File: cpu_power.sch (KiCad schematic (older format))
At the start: 81 parts

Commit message: annotation, wip erc
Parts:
- removed C? (x4): 100nF/6.3V, symbol C
- added C70, C72, C74, C75: 100nF/6.3V, symbol C
- gave numbers to parts that had none: 77

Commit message: erc passed, sch first version
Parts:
- W1: value VDD_MPUON -> VDD_MPU_MON
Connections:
- wire segments 234 -> 238
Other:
- note added: "VDD_MPU_MON connected to VDD_MPU \naccording to Fig 6-7 of AM335x datasheet."
- moved on the sheet: W1

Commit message: wip sys and power
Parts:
- removed C100, C101, C102, C103, C104, C105, C106, C107, C108, C109, C110, C43, C45, C46, C48, C50, C51, C52, C53, C54, C55, C56, C57, C58, C59, C60, C61, C62, C63, C64, C65, C66, C67, C68, C69, C70, C71, C72, C73, C74, C75, C77, C78, C79, C80, C81, C82, C83, C84, C86, C87, C88, C89, C90, C91, C92, C94, C96, C97, C98, C99: 100nF/6.3V, symbol C
- removed C111, C112, C113, C114, C115: 1uF/10V, symbol C
- removed C44, C47, C76, C85, C93, C95: 10uF/10V, symbol C
- removed C49: 1nF/50V, symbol C
- removed IC2: AM335X_ZCZ, symbol AM335X_ZCZ
- removed L5, L6, L7: 150OHM800mA, symbol L
- removed R29, R30, R31: 0R, symbol R
- removed W1: VDD_MPU_MON, symbol TEST_1P
- added IC? (x2): OSD335x, GHI-SoMs-Processors_OSD3358, symbol OSD335x
- added R?: 10k 1%, symbol R
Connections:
- net labels removed: GND_OSC, VDDS, VSS_RTC
- wire segments 238 -> 104
- no-connect marks 1 -> 65
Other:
- note removed: "VDD_MPU_MON connected to VDD_MPU \naccording to Fig 6-7 of AM335x datasheet."

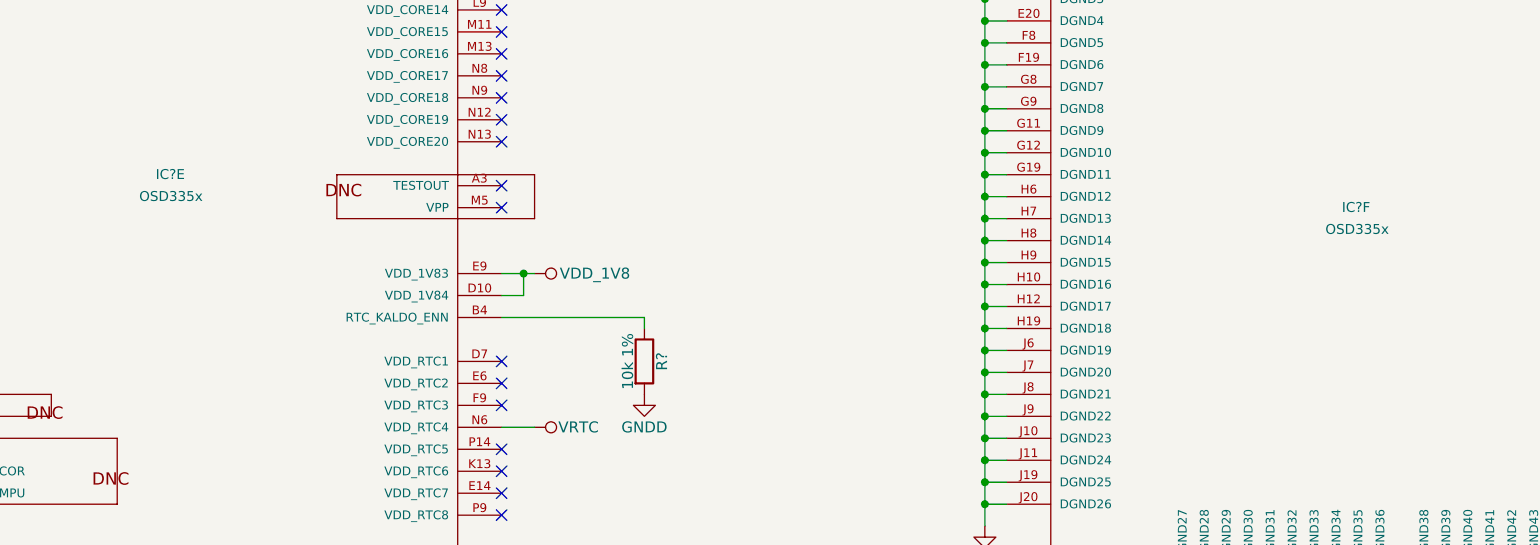
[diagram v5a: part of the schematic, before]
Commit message: only io connectors remaining
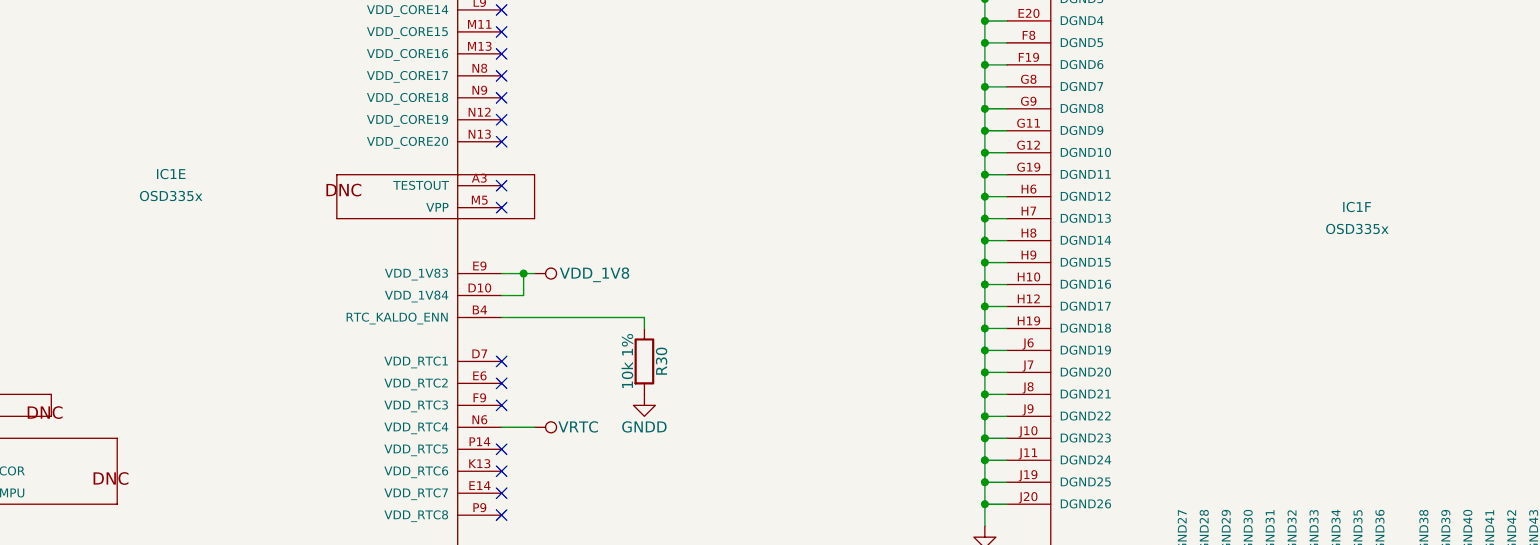
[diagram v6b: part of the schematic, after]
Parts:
- gave numbers to parts that had none: 2
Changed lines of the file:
@@
 $Descr A4 11693 8268
 encoding utf-8
-Sheet 5 6
+Sheet 4 6
 Title ""
 Date ""
@@
 $EndDescr
 $Comp
-L OSD335x IC?
+L OSD335x IC1
 U 5 1 58DDF956
 P 3200 3550
-F 0 "IC?" H 3125 3575 45  0000 L BNN
+F 0 "IC1" H 3125 3575 45  0000 L BNN
 F 1 "OSD335x" H 3050 3475 45  0000 L BNN
 F 2 "GHI-SoMs-Processors_OSD3358" H 3230 3700 20  0001 C CNN
@@
 $EndComp
 $Comp
-L OSD335x IC?
+L OSD335x IC1
 U 6 1 58DDF9B7
 P 8600 3700
-F 0 "IC?" H 8525 3725 45  0000 L BNN
+F 0 "IC1" H 8525 3725 45  0000 L BNN
 F 1 "OSD335x" H 8450 3625 45  0000 L BNN
 F 2 "GHI-SoMs-Processors_OSD3358" H 8630 3850 20  0001 C CNN
@@
 	6900 5000 7000 5000
 $Comp
-L GNDD #PWR?
+L GNDD #PWR66
 U 1 1 58E11DA7
 P 6900 5100
-F 0 "#PWR?" H 6900 4850 50  0001 C CNN
+F 0 "#PWR66" H 6900 4850 50  0001 C CNN
 F 1 "GNDD" H 6900 4950 50  0000 C CNN
 F 2 "" H 6900 5100 50  0001 C CNN
@@
 	10300 5000 10200 5000
 $Comp
-L GNDD #PWR?
+L GNDD #PWR69
 U 1 1 58E11EBE
 P 10300 5100
-F 0 "#PWR?" H 10300 4850 50  0001 C CNN
+F 0 "#PWR69" H 10300 4850 50  0001 C CNN
 F 1 "GNDD" H 10300 4950 50  0000 C CNN
 F 2 "" H 10300 5100 50  0001 C CNN
@@
 	7800 5500 7800 5650
 $Comp
-L GNDD #PWR?
+L GNDD #PWR67
 U 1 1 58E12353
 P 7800 5650
-F 0 "#PWR?" H 7800 5400 50  0001 C CNN
+F 0 "#PWR67" H 7800 5400 50  0001 C CNN
 F 1 "GNDD" H 7800 5500 50  0000 C CNN
 F 2 "" H 7800 5650 50  0001 C CNN
@@
 Connection ~ 7800 5600
 $Comp
-L GNDA #PWR?
+L GNDA #PWR68
 U 1 1 58E12456
 P 9700 5600
-F 0 "#PWR?" H 9700 5350 50  0001 C CNN
+F 0 "#PWR68" H 9700 5350 50  0001 C CNN
 F 1 "GNDA" H 9700 5450 50  0000 C CNN
 F 2 "" H 9700 5600 50  0001 C CNN
@@
 Connection ~ 1600 2950
 $Comp
-L VDD_3V3A #PWR?
+L VDD_3V3A #PWR57
 U 1 1 58E148B3
 P 1400 2850
-F 0 "#PWR?" H 1400 2700 50  0001 C CNN
+F 0 "#PWR57" H 1400 2700 50  0001 C CNN
 F 1 "VDD_3V3A" V 1400 3150 50  0000 C CNN
 F 2 "" H 1400 2850 50  0000 C CNN
@@
 Connection ~ 1600 2850
 $Comp
-L VDD_MPU #PWR?
+L VDD_MPU #PWR60
 U 1 1 58E14A82
 P 1600 3750
-F 0 "#PWR?" H 1600 3600 50  0001 C CNN
+F 0 "#PWR60" H 1600 3600 50  0001 C CNN
 F 1 "VDD_MPU" V 1600 4025 50  0000 C CNN
 F 2 "" H 1600 3750 50  0000 C CNN
@@
 	1600 3750 1700 3750
 $Comp
-L VDD_ADC #PWR?
+L VDD_ADC #PWR58
 U 1 1 58E14B9C
 P 1400 5050
-F 0 "#PWR?" H 1400 4900 50  0001 C CNN
+F 0 "#PWR58" H 1400 4900 50  0001 C CNN
 F 1 "VDD_ADC" V 1400 5325 50  0000 C CNN
 F 2 "" H 1400 5050 50  0000 C CNN
@@
 	1700 5050 1400 5050
 $Comp
-L VDD_PLL #PWR?
+L VDD_PLL #PWR59
 U 1 1 58E14C7B
 P 1400 5250
-F 0 "#PWR?" H 1400 5100 50  0001 C CNN
+F 0 "#PWR59" H 1400 5100 50  0001 C CNN
 F 1 "VDD_PLL" V 1400 5525 50  0000 C CNN
 F 2 "" H 1400 5250 50  0000 C CNN
@@
 NoConn ~ 1700 4950
 $Comp
-L VDD_CORE #PWR?
+L VDD_CORE #PWR64
 U 1 1 58E150D4
 P 4900 1450
-F 0 "#PWR?" H 4900 1300 50  0001 C CNN
+F 0 "#PWR64" H 4900 1300 50  0001 C CNN
 F 1 "VDD_CORE" V 4900 1750 50  0000 C CNN
 F 2 "" H 4900 1450 50  0000 C CNN
@@
 NoConn ~ 4700 3650
 $Comp
-L VRTC #PWR?
+L VRTC #PWR62
 U 1 1 58E1525D
 P 4850 4650
-F 0 "#PWR?" H 4850 4500 50  0001 C CNN
+F 0 "#PWR62" H 4850 4500 50  0001 C CNN
 F 1 "VRTC" V 4850 4850 50  0000 C CNN
 F 2 "" H 4850 4650 50  0000 C CNN
@@
 	4850 4650 4700 4650
 $Comp
-L R R?
+L R R30
 U 1 1 58E1536B
 P 5350 4350
-F 0 "R?" V 5430 4350 50  0000 C CNN
+F 0 "R30" V 5430 4350 50  0000 C CNN
 F 1 "10k 1%" V 5275 4350 50  0000 C CNN
 F 2 "" V 5280 4350 50  0001 C CNN
@@
 $EndComp
 $Comp
-L GNDD #PWR?
+L GNDD #PWR65
 U 1 1 58E153CC
 P 5350 4500
-F 0 "#PWR?" H 5350 4250 50  0001 C CNN
+F 0 "#PWR65" H 5350 4250 50  0001 C CNN
 F 1 "GNDD" H 5350 4350 50  0000 C CNN
 F 2 "" H 5350 4500 50  0001 C CNN
@@
 NoConn ~ 4700 5050
 $Comp
-L VDDS_DDR #PWR?
+L VDDS_DDR #PWR63
 U 1 1 58E1559B
 P 4850 5550
-F 0 "#PWR?" H 4850 5400 50  0001 C CNN
+F 0 "#PWR63" H 4850 5400 50  0001 C CNN
 F 1 "VDDS_DDR" V 4850 5850 50  0000 C CNN
 F 2 "" H 4850 5550 50  0000 C CNN
@@
 NoConn ~ 4700 5850
 $Comp
-L VDD_1V8 #PWR?
+L VDD_1V8 #PWR61
 U 1 1 58E16271
 P 4850 3950
-F 0 "#PWR?" H 4850 3800 50  0001 C CNN
+F 0 "#PWR61" H 4850 3800 50  0001 C CNN
 F 1 "VDD_1V8" V 4850 4225 50  0000 C CNN
 F 2 "" H 4850 3950 50  0000 C CNN

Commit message: erc passed
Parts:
- added J15: VDDS_PLL, symbol TEST_1P
- added J16: VDDS_DDR, symbol TEST_1P
- added J17: VDD_MPU, symbol TEST_1P
- added J18: VDD_CORE, symbol TEST_1P
- IC1: symbol OSD335x -> OSD335x-RESCUE-mateboard
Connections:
- net VDDS_DDR: no longer names the net of IC1.H5 (VDDS_DDR4)
- net VDDS_DDR: now also J16.1
- net VDD_CORE: no longer names the net of IC1.F6 (VDD_CORE1)
- net VDD_CORE: now also J18.1
- net VDD_MPU: no longer names the net of IC1.F10 (VDD_MPU0)
- net VDD_MPU: now also J17.1
- net VDD_PLL: no longer names the net of IC1.E7 (VDD_PLL1)
- net VDD_PLL: now also J15.1
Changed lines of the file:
@@
 $EndDescr
 $Comp
-L OSD335x IC1
+L OSD335x-RESCUE-mateboard IC1
 U 5 1 58DDF956
 P 3200 3550
+AR Path="/58DDF956" Ref="IC1"  Part="5"
+AR Path="/589E2993/58DDF956" Ref="IC1"  Part="5"
 F 0 "IC1" H 3125 3575 45  0000 L BNN
 F 1 "OSD335x" H 3050 3475 45  0000 L BNN
@@
 $EndComp
 $Comp
-L OSD335x IC1
+L OSD335x-RESCUE-mateboard IC1
 U 6 1 58DDF9B7
 P 8600 3700
+AR Path="/58DDF9B7" Ref="IC1"  Part="6"
+AR Path="/589E2993/58DDF9B7" Ref="IC1"  Part="6"
 F 0 "IC1" H 8525 3725 45  0000 L BNN
 F 1 "OSD335x" H 8450 3625 45  0000 L BNN
@@
 	6900 5000 7000 5000
 $Comp
-L GNDD #PWR66
+L GNDD #PWR094
 U 1 1 58E11DA7
 P 6900 5100
-F 0 "#PWR66" H 6900 4850 50  0001 C CNN
+F 0 "#PWR094" H 6900 4850 50  0001 C CNN
 F 1 "GNDD" H 6900 4950 50  0000 C CNN
 F 2 "" H 6900 5100 50  0001 C CNN
@@
 	10300 5000 10200 5000
 $Comp
-L GNDD #PWR69
+L GNDD #PWR095
 U 1 1 58E11EBE
 P 10300 5100
-F 0 "#PWR69" H 10300 4850 50  0001 C CNN
+F 0 "#PWR095" H 10300 4850 50  0001 C CNN
 F 1 "GNDD" H 10300 4950 50  0000 C CNN
 F 2 "" H 10300 5100 50  0001 C CNN
@@
 Connection ~ 9400 5600
 Wire Wire Line
-	9500 5500 9500 5600
-Wire Wire Line
-	9500 5600 7800 5600
+	9500 5600 9500 5500
+Wire Wire Line
+	7800 5600 9500 5600
 Wire Wire Line
 	7800 5500 7800 5650
 $Comp
-L GNDD #PWR67
+L GNDD #PWR096
 U 1 1 58E12353
 P 7800 5650
-F 0 "#PWR67" H 7800 5400 50  0001 C CNN
+F 0 "#PWR096" H 7800 5400 50  0001 C CNN
 F 1 "GNDD" H 7800 5500 50  0000 C CNN
 F 2 "" H 7800 5650 50  0001 C CNN
@@
 Connection ~ 7800 5600
 $Comp
-L GNDA #PWR68
+L GNDA #PWR097
 U 1 1 58E12456
 P 9700 5600
-F 0 "#PWR68" H 9700 5350 50  0001 C CNN
+F 0 "#PWR097" H 9700 5350 50  0001 C CNN
 F 1 "GNDA" H 9700 5450 50  0000 C CNN
 F 2 "" H 9700 5600 50  0001 C CNN
@@
 $EndComp
 Wire Wire Line
-	9700 5600 9700 5500
+	9700 5500 9700 5600
 Wire Wire Line
 	1600 3050 1700 3050
@@
 Connection ~ 1600 2950
 $Comp
-L VDD_3V3A #PWR57
+L VDD_3V3A #PWR098
 U 1 1 58E148B3
 P 1400 2850
-F 0 "#PWR57" H 1400 2700 50  0001 C CNN
+F 0 "#PWR098" H 1400 2700 50  0001 C CNN
 F 1 "VDD_3V3A" V 1400 3150 50  0000 C CNN
 F 2 "" H 1400 2850 50  0000 C CNN
@@
 $EndComp
 Connection ~ 1600 2850
-$Comp
-L VDD_MPU #PWR60
-U 1 1 58E14A82
-P 1600 3750
-F 0 "#PWR60" H 1600 3600 50  0001 C CNN
-F 1 "VDD_MPU" V 1600 4025 50  0000 C CNN
-F 2 "" H 1600 3750 50  0000 C CNN
-F 3 "" H 1600 3750 50  0000 C CNN
-	1    1600 3750
-	0    -1   -1   0
-$EndComp
-Wire Wire Line
-	1600 3750 1700 3750
-$Comp
-L VDD_ADC #PWR58
+Wire Wire Line
+	1550 3750 1700 3750
+$Comp
+L VDD_ADC #PWR099
 U 1 1 58E14B9C
 P 1400 5050
-F 0 "#PWR58" H 1400 4900 50  0001 C CNN
+F 0 "#PWR099" H 1400 4900 50  0001 C CNN
 F 1 "VDD_ADC" V 1400 5325 50  0000 C CNN
 F 2 "" H 1400 5050 50  0000 C CNN
@@
 Wire Wire Line
 	1700 5050 1400 5050
-$Comp
-L VDD_PLL #PWR59
-U 1 1 58E14C7B
-P 1400 5250
-F 0 "#PWR59" H 1400 5100 50  0001 C CNN
-F 1 "VDD_PLL" V 1400 5525 50  0000 C CNN
-F 2 "" H 1400 5250 50  0000 C CNN
-F 3 "" H 1400 5250 50  0000 C CNN
-	1    1400 5250
-	0    -1   -1   0
-$EndComp
 Wire Wire Line
 	1400 5250 1700 5250
@@
 NoConn ~ 1700 4850
 NoConn ~ 1700 4950
-$Comp
-L VDD_CORE #PWR64
-U 1 1 58E150D4
-P 4900 1450
-F 0 "#PWR64" H 4900 1300 50  0001 C CNN
-F 1 "VDD_CORE" V 4900 1750 50  0000 C CNN
-F 2 "" H 4900 1450 50  0000 C CNN
-F 3 "" H 4900 1450 50  0000 C CNN
-	1    4900 1450
-	0    1    1    0
-$EndComp
 Wire Wire Line
 	4900 1450 4700 1450
@@
 NoConn ~ 4700 3550
 NoConn ~ 4700 3650
-$Comp
-L VRTC #PWR62
-U 1 1 58E1525D
-P 4850 4650
-F 0 "#PWR62" H 4850 4500 50  0001 C CNN
-F 1 "VRTC" V 4850 4850 50  0000 C CNN
-F 2 "" H 4850 4650 50  0000 C CNN
-F 3 "" H 4850 4650 50  0000 C CNN
-	1    4850 4650
-	0    1    1    0
-$EndComp
 Wire Wire Line
 	4850 4650 4700 4650
@@
 $EndComp
 $Comp
-L GNDD #PWR65
+L GNDD #PWR0100
 U 1 1 58E153CC
 P 5350 4500
-F 0 "#PWR65" H 5350 4250 50  0001 C CNN
+F 0 "#PWR0100" H 5350 4250 50  0001 C CNN
 F 1 "GNDD" H 5350 4350 50  0000 C CNN
 F 2 "" H 5350 4500 50  0001 C CNN
@@
 NoConn ~ 4700 4950
 NoConn ~ 4700 5050
-$Comp
-L VDDS_DDR #PWR63
-U 1 1 58E1559B
-P 4850 5550
-F 0 "#PWR63" H 4850 5400 50  0001 C CNN
-F 1 "VDDS_DDR" V 4850 5850 50  0000 C CNN
-F 2 "" H 4850 5550 50  0000 C CNN
-F 3 "" H 4850 5550 50  0000 C CNN
-	1    4850 5550
-	0    1    1    0
-$EndComp
 Wire Wire Line
 	4850 5550 4700 5550
@@
 NoConn ~ 4700 5850
 $Comp
-L VDD_1V8 #PWR61
+L VDD_1V8 #PWR0101
 U 1 1 58E16271
 P 4850 3950
-F 0 "#PWR61" H 4850 3800 50  0001 C CNN
+F 0 "#PWR0101" H 4850 3800 50  0001 C CNN
 F 1 "VDD_1V8" V 4850 4225 50  0000 C CNN
 F 2 "" H 4850 3950 50  0000 C CNN
@@
 $EndComp
 Wire Wire Line
-	4850 3950 4700 3950
+	4700 3950 4850 3950
 Wire Wire Line
 	4800 3950 4800 4050
@@
 	4800 4050 4700 4050
 Connection ~ 4800 3950
+$Comp
+L PWR_FLAG #FLG0102
+U 1 1 58DCC8EE
+P 9700 5550
+F 0 "#FLG0102" H 9700 5625 50  0001 C CNN
+F 1 "PWR_FLAG" H 9700 5700 50  0001 C CNN
+F 2 "" H 9700 5550 50  0001 C CNN
+F 3 "" H 9700 5550 50  0001 C CNN
+	1    9700 5550
+	0    1    1    0
+$EndComp
+Connection ~ 9700 5550
+$Comp
+L TEST_1P J15
+U 1 1 58DD0E89
+P 1400 5250
+F 0 "J15" V 1425 5300 50  0000 C CNN
+F 1 "VDDS_PLL" V 1400 5600 50  0000 C CNN
+F 2 "" H 1600 5250 50  0001 C CNN
+F 3 "" H 1600 5250 50  0001 C CNN
+	1    1400 5250
+	0    -1   -1   0
+$EndComp
+$Comp
+L TEST_1P J16
+U 1 1 58DD1032
+P 4850 5550
+F 0 "J16" V 4800 5600 50  0000 C CNN
+F 1 "VDDS_DDR" V 4850 5925 50  0000 C CNN
+F 2 "" H 5050 5550 50  0001 C CNN
+F 3 "" H 5050 5550 50  0001 C CNN
+	1    4850 5550
+	0    1    1    0
+$EndComp
+$Comp
+L PWR_FLAG #FLG0103
+U 1 1 58DD740C
+P 1600 2850
+F 0 "#FLG0103" H 1600 2925 50  0001 C CNN
+F 1 "PWR_FLAG" H 1600 3000 50  0001 C CNN
+F 2 "" H 1600 2850 50  0001 C CNN
+F 3 "" H 1600 2850 50  0001 C CNN
+	1    1600 2850
+	1    0    0    -1
+$EndComp
+$Comp
+L PWR_FLAG #FLG0104
+U 1 1 58DD798F
+P 7800 5600
+F 0 "#FLG0104" H 7800 5675 50  0001 C CNN
+F 1 "PWR_FLAG" H 7800 5750 50  0001 C CNN
+F 2 "" H 7800 5600 50  0001 C CNN
+F 3 "" H 7800 5600 50  0001 C CNN
+	1    7800 5600
+	0    -1   -1   0
+$EndComp
+$Comp
+L TEST_1P J17
+U 1 1 58DDD69E
+P 1550 3750
+F 0 "J17" V 1600 3800 50  0000 C CNN
+F 1 "VDD_MPU" V 1550 4100 50  0000 C CNN
+F 2 "" H 1750 3750 50  0001 C CNN
+F 3 "" H 1750 3750 50  0001 C CNN
+	1    1550 3750
+	0    -1   -1   0
+$EndComp
+$Comp
+L VRTC #PWR0105
+U 1 1 58E1525D
+P 4850 4650
+F 0 "#PWR0105" H 4850 4500 50  0001 C CNN
+F 1 "VRTC" V 4850 4850 50  0000 C CNN
+F 2 "" H 4850 4650 50  0000 C CNN
+F 3 "" H 4850 4650 50  0000 C CNN
+	1    4850 4650
+	0    1    1    0
+$EndComp
+$Comp
+L TEST_1P J18
+U 1 1 58DDEA58
+P 4900 1450
+F 0 "J18" V 4850 1500 50  0000 C CNN
+F 1 "VDD_CORE" V 4900 1825 50  0000 C CNN
+F 2 "" H 5100 1450 50  0001 C CNN
+F 3 "" H 5100 1450 50  0001 C CNN
+	1    4900 1450
+	0    1    1    0
+$EndComp
 $EndSCHEMATC

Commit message: wip footprint assoc
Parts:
- IC1: footprint GHI-SoMs-Processors_OSD3358 -> footprints:OSD3358-BAS-BGA400
- J15, J16, J17, J18: footprint (none) -> Measurement_Points:Measurement_Point_Round-SMD-Pad_Small
- R30: footprint (none) -> Resistors_SMD:R_0402
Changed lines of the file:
@@
 F 0 "IC1" H 3125 3575 45  0000 L BNN
 F 1 "OSD335x" H 3050 3475 45  0000 L BNN
-F 2 "GHI-SoMs-Processors_OSD3358" H 3230 3700 20  0001 C CNN
+F 2 "footprints:OSD3358-BAS-BGA400" H 3230 3700 20  0001 C CNN
 F 3 "" H 3200 3550 60  0001 C CNN
 	5    3200 3550
@@
 F 0 "IC1" H 8525 3725 45  0000 L BNN
 F 1 "OSD335x" H 8450 3625 45  0000 L BNN
-F 2 "GHI-SoMs-Processors_OSD3358" H 8630 3850 20  0001 C CNN
+F 2 "footprints:OSD3358-BAS-BGA400" H 8630 3850 20  0001 C CNN
 F 3 "" H 8600 3700 60  0001 C CNN
 	6    8600 3700
@@
 F 0 "R30" V 5430 4350 50  0000 C CNN
 F 1 "10k 1%" V 5275 4350 50  0000 C CNN
-F 2 "" V 5280 4350 50  0001 C CNN
+F 2 "Resistors_SMD:R_0402" V 5280 4350 50  0001 C CNN
 F 3 "" H 5350 4350 50  0001 C CNN
 	1    5350 4350
@@
 F 0 "J15" V 1425 5300 50  0000 C CNN
 F 1 "VDDS_PLL" V 1400 5600 50  0000 C CNN
-F 2 "" H 1600 5250 50  0001 C CNN
+F 2 "Measurement_Points:Measurement_Point_Round-SMD-Pad_Small" H 1600 5250 50  0001 C CNN
 F 3 "" H 1600 5250 50  0001 C CNN
 	1    1400 5250
@@
 F 0 "J16" V 4800 5600 50  0000 C CNN
 F 1 "VDDS_DDR" V 4850 5925 50  0000 C CNN
-F 2 "" H 5050 5550 50  0001 C CNN
+F 2 "Measurement_Points:Measurement_Point_Round-SMD-Pad_Small" H 5050 5550 50  0001 C CNN
 F 3 "" H 5050 5550 50  0001 C CNN
 	1    4850 5550
@@
 F 0 "J17" V 1600 3800 50  0000 C CNN
 F 1 "VDD_MPU" V 1550 4100 50  0000 C CNN
-F 2 "" H 1750 3750 50  0001 C CNN
+F 2 "Measurement_Points:Measurement_Point_Round-SMD-Pad_Small" H 1750 3750 50  0001 C CNN
 F 3 "" H 1750 3750 50  0001 C CNN
 	1    1550 3750
@@
 F 0 "J18" V 4850 1500 50  0000 C CNN
 F 1 "VDD_CORE" V 4900 1825 50  0000 C CNN
-F 2 "" H 5100 1450 50  0001 C CNN
+F 2 "Measurement_Points:Measurement_Point_Round-SMD-Pad_Small" H 5100 1450 50  0001 C CNN
 F 3 "" H 5100 1450 50  0001 C CNN
 	1    4900 1450
